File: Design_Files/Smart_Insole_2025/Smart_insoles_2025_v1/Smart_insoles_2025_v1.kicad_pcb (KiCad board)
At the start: 4 copper layers, 69.7 x 30.1 mm, 88 parts, among them IC1 USBLC6-2SC6, J1 Conn_01x20, J2 USB_C_Receptacle_USB2.0_16P, J4 S2B-PH-SM4-TB_LF__SN_, Q2 FDN306P, SW1 RESET, SW2 BOOT, SW3 SW_Nidec_CAS-120A1, U1 ME6211C33M5, U2 CD74HC4067M96, U3 LSM6DSO32TR, U5 ESP32-C3-MINI-1-N4, U7 BQ24040DSQR, U8 MCP6004-I_ST, U9 MCP6004-I_ST

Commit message: PCB:new routing-p1
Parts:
- C14, C15, C24, RN1, U3: moved to B.Cu
- moved J4 45.5 mm to (115.5, 83.7)
- moved SW3 24.8 mm to (154.8, 96.9), turned to 180 degrees
- moved C22 19.8 mm to (141.2, 83.2)
- moved D2 19.8 mm to (150.2, 83.2)
- moved R28 19.8 mm to (147.7, 83.2)
- moved U1 19.8 mm to (144.6, 83.2)
- moved C23 19.8 mm to (144.7, 86.2)
- moved R13 19.4 mm to (123.3, 89.5)
- moved R27 19.4 mm to (123.3, 87.5)
- moved JP2 18.1 mm to (124.5, 92.5)
- moved C16 17.7 mm to (129.2, 89.6)
- moved C19 17.7 mm to (133.4, 87.0)
- moved R20 17.7 mm to (138.2, 87.0)
- moved R21 17.7 mm to (135.8, 87.0)
- moved D1 17.7 mm to (135.8, 83.3)
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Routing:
- net +3V3: track 55.8 -> 117.3 mm, vias 0 -> 3
- net /FSR_AnalogFE/FSR_OUT_7: track 76.8 -> 15.8 mm, vias 2 -> 0
- net /FSR_AnalogFE/FSR_OUT_6: track 65.2 -> 14.9 mm
- net GND: track 159.3 -> 121.9 mm, vias 84 -> 74
- net I7: track 11.1 -> 45.7 mm, vias 1 -> 4
- net VBUS: track 54.8 -> 22.2 mm
- net /Battery Circuit Options/VBat: track 19.7 -> 49.1 mm
- net /FSR_AnalogFE/FSR_OUT_5: track 43.9 -> 19.5 mm
- net S1: track 2.04 -> 24.5 mm, vias 1 -> 0
- net S0: track 2.00 -> 22.6 mm, vias 1 -> 0
- net /FSR_AnalogFE/FSR_OUT_4: track 30.5 -> 10.8 mm
- net /Battery Circuit Options/~{PG}: track 0.00 -> 18.9 mm
- net S2: track 22.1 -> 4.63 mm
- net S3: track 22.1 -> 4.74 mm
- net /FSR_AnalogFE/FSR_OUT_0: track 29.0 -> 15.5 mm
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
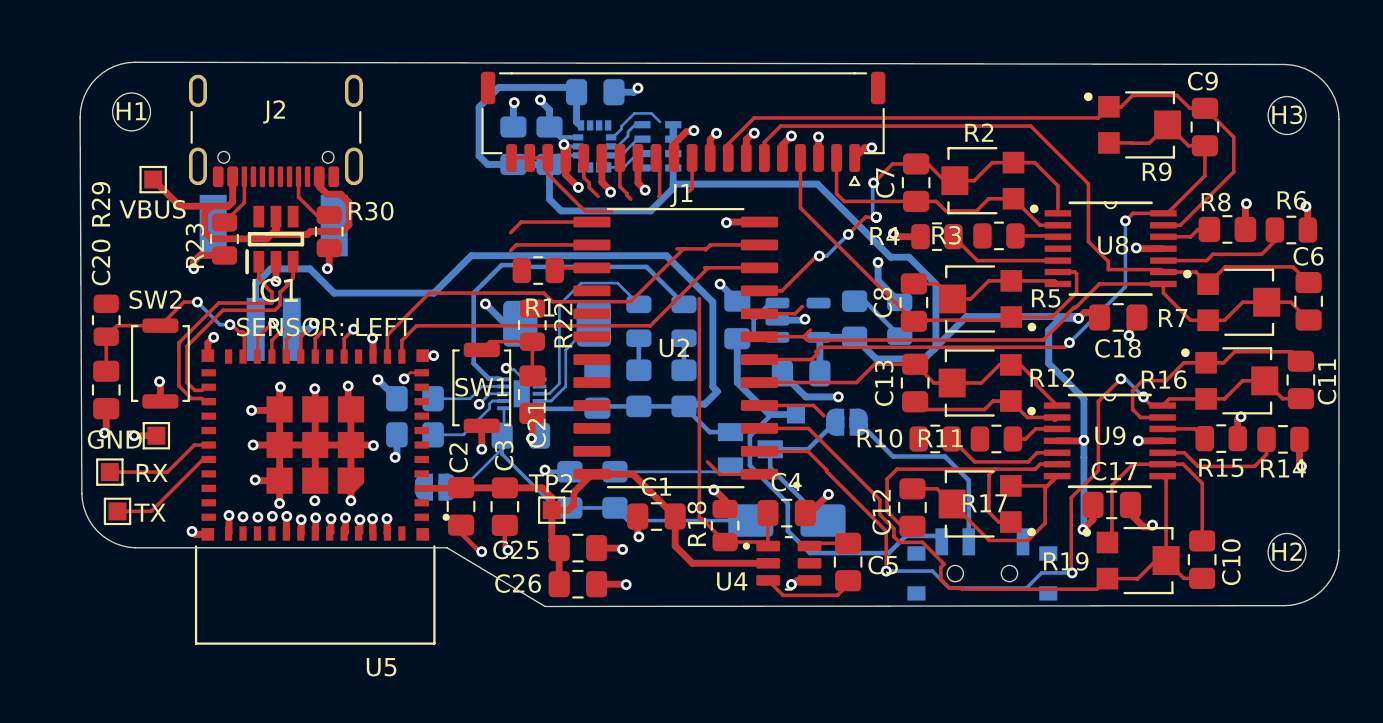
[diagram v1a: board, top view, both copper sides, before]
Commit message: PCB: finished routing single ended signal. Pending usb differential pair
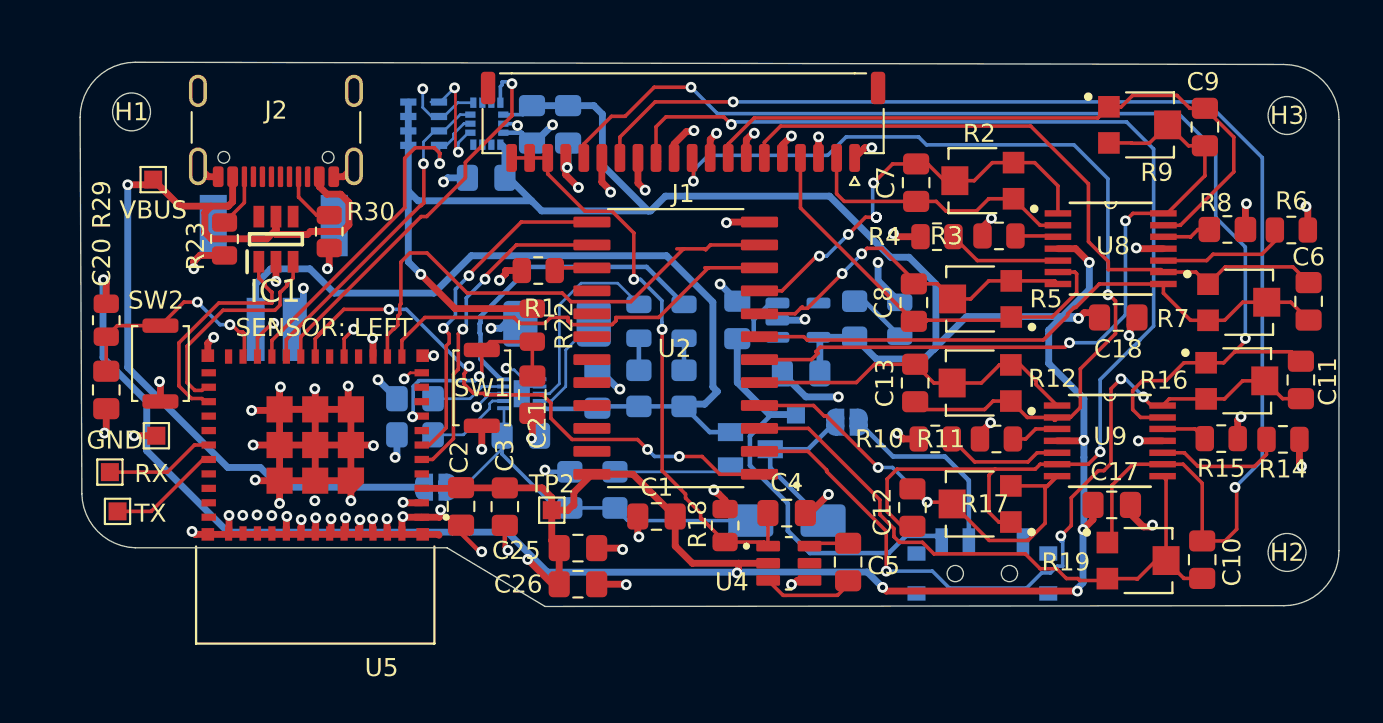
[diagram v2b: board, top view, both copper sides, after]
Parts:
- moved RN1 13.0 mm to (123.8, 72.3), turned to 180 degrees
- moved C24 7.68 mm to (127.3, 75.3), turned to 180 degrees
- moved U3 6.10 mm to (127.3, 72.3), turned to -90 degrees
- moved C14 3.25 mm to (131.8, 72.4), turned to -90 degrees
- moved C15 1.53 mm to (129.8, 72.4), turned to -90 degrees
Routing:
- net +3V3: track 117.3 -> 212.8 mm, vias 3 -> 10
- net /FSR_AnalogFE/FSR_OUT_6: track 14.9 -> 74.6 mm, vias 0 -> 2
- net /FSR_AnalogFE/FSR_OUT_5: track 19.5 -> 68.7 mm, vias 0 -> 2
- net /FSR_AnalogFE/FSR_OUT_7: track 15.8 -> 63.9 mm, vias 0 -> 2
- net /FSR_AnalogFE/FSR_OUT_4: track 10.8 -> 50.9 mm, vias 0 -> 2
- net GND: track 121.9 -> 158.4 mm, vias 74 -> 85
- net VBUS: track 22.2 -> 53.0 mm, vias 0 -> 1
- net SIG: track 4.68 -> 31.9 mm, vias 0 -> 4
- net INT: track 1.55 -> 22.0 mm, vias 0 -> 1
- net SCL: track 4.14 -> 20.5 mm, vias 0 -> 1
- net SDA: track 3.44 -> 18.3 mm, vias 0 -> 1
- net S3: track 4.74 -> 19.1 mm, vias 0 -> 2
- net S2: track 4.63 -> 18.8 mm, vias 0 -> 2
- net I1: track 11.3 -> 19.9 mm, vias 0 -> 2
- net I5: track 18.4 -> 26.1 mm, vias 0 -> 2
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
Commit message: SCH:Added pullup resistors on strapping pins.Added 0.1uF on analog input. Added testpoint on missing pad. PCB:Placed new components.Routing refactoring p1
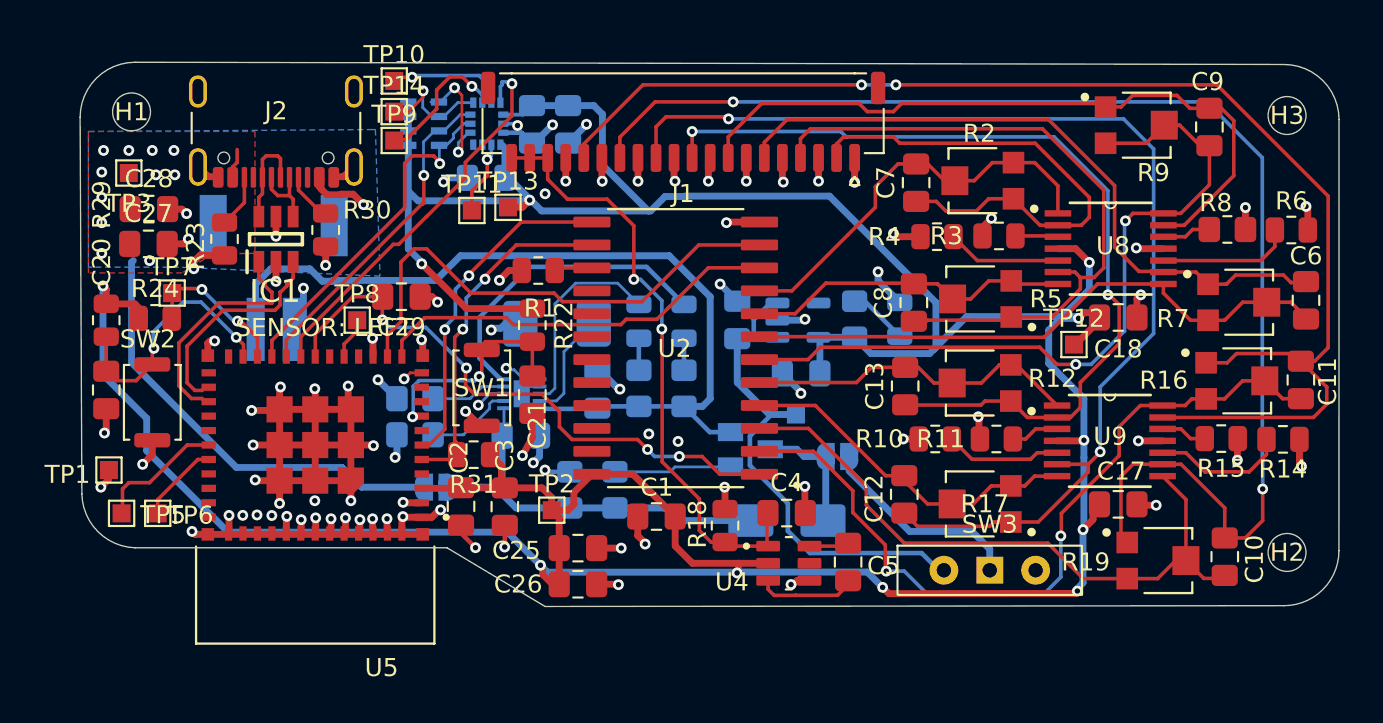
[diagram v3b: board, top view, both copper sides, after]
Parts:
- added C27: 0.1uF, Capacitor_SMD:C_0805_2012Metric_Pad1.18x1.45mm_HandSolder, F.Cu at (108.6, 79.0)
- added C28: 10uF, Capacitor_SMD:C_0805_2012Metric_Pad1.18x1.45mm_HandSolder, F.Cu at (108.6, 77.0)
- added C29: 0.1uF, Capacitor_SMD:C_0805_2012Metric_Pad1.18x1.45mm_HandSolder, F.Cu at (122.6, 81.9)
- added R24: 10k, Resistor_SMD:R_0805_2012Metric, F.Cu at (109.0, 83.1)
- added R31: 10k, Resistor_SMD:R_0805_2012Metric, F.Cu at (126.6, 90.7)
- added TP10: TestPoint_Alt, TestPoint:TestPoint_Pad_1.0x1.0mm, F.Cu at (122.2, 70.0)
- added TP11: TestPoint_Alt, TestPoint:TestPoint_Pad_1.0x1.0mm, F.Cu at (126.5, 77.1)
- added TP12: TestPoint_Alt, TestPoint:TestPoint_Pad_1.0x1.0mm, F.Cu at (159.8, 84.5)
- added TP13: TestPoint_Alt, TestPoint:TestPoint_Pad_1.0x1.0mm, F.Cu at (128.5, 77.0)
- added TP14: TestPoint_Alt, TestPoint:TestPoint_Pad_1.0x1.0mm, F.Cu at (122.2, 71.7)
- added TP7: TestPoint_Alt, TestPoint:TestPoint_Pad_1.0x1.0mm, F.Cu at (109.9, 81.7)
- added TP8: TestPoint_Alt, TestPoint:TestPoint_Pad_1.0x1.0mm, F.Cu at (120.2, 83.2)
- added TP9: TestPoint_Alt, TestPoint:TestPoint_Pad_1.0x1.0mm, F.Cu at (122.2, 73.2)
- C21: value 0.1uF -> 1uF
- SW3: footprint Button_Switch_SMD:SW_SPDT_PCM12 -> Button_Switch_THT:SW_Slide-03_Wuerth-WS-SLTV_10x2.5x6.4_P2.54mm; moved to F.Cu
- moved TP1 3.24 mm to (106.4, 91.5)
- moved TP5 2.38 mm to (107.1, 93.9)
- moved TP6 2.23 mm to (109.1, 93.9)
- moved SW2 2.19 mm to (108.8, 87.8)
- moved JP1 1.97 mm to (146.8, 90.8)
- moved TP3 1.40 mm to (107.5, 75.0)
- moved C10 1.26 mm to (168.2, 96.3)
- moved R19 1.10 mm to (164.6, 96.5)
- moved C12 0.86 mm to (150.4, 92.8)
- moved C13 0.58 mm to (150.5, 86.8)
- moved SW3 0.43 mm to (155.2, 97.0), turned to 0 degrees
- moved C17 0.36 mm to (162.3, 93.4)
- moved C9 0.25 mm to (167.3, 72.5)
- moved R30 0.22 mm to (118.4, 78.2)
- moved R9 0.19 mm to (163.4, 72.4)
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- renumbered GND to TP1, VBUS to TP3, RX to TP5, TX to TP6
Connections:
- net /Battery Circuit Options/IN renamed /Battery Circuit Options/VBUS_IN
- net Net-(D5-K) renamed /Battery Circuit Options/VBUS_OUT_A
- net Net-(JP1-B) renamed /Battery Circuit Options/VBUS_OUT_B
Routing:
- net VBUS: track 53.0 -> 31.0 mm, vias 1 -> 13
- net /FSR_AnalogFE/FSR_OUT_1: track 23.4 -> 37.3 mm
- net /FSR_AnalogFE/FSR_OUT_0: track 15.5 -> 28.3 mm
- net /FSR_AnalogFE/FSR_OUT_7: track 63.9 -> 74.2 mm
- net SDX: track 0.00 -> 7.79 mm, vias 0 -> 1
- net SCX: track 0.00 -> 7.45 mm, vias 0 -> 1
- net I5: track 26.1 -> 19.2 mm, vias 2 -> 0
- net IO8: track 2.27 -> 8.46 mm, vias 1 -> 2
- net +3V3: track 212.8 -> 218.6 mm, vias 10 -> 11
- net /USB_TVS_P: track 0.00 -> 5.40 mm
- net /FSR_AnalogFE/FSR_OUT_5: track 68.7 -> 63.9 mm
- net /USB_TVS_N: track 0.00 -> 4.13 mm
- net INT2: track 0.00 -> 4.09 mm, vias 0 -> 1
- net GND: track 158.4 -> 155.7 mm, vias 85 -> 92
- net /Battery Circuit Options/VBUS_OUT_A: track 9.38 -> 6.85 mm
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- added copper zone on B.Cu, net VBUS
- added copper zone on F.Cu, net VBUS

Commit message: PCB: Routing refactoring. Moved Multiplexer to the right. Organized Silkscreen p1. USB DIFF NOT READY
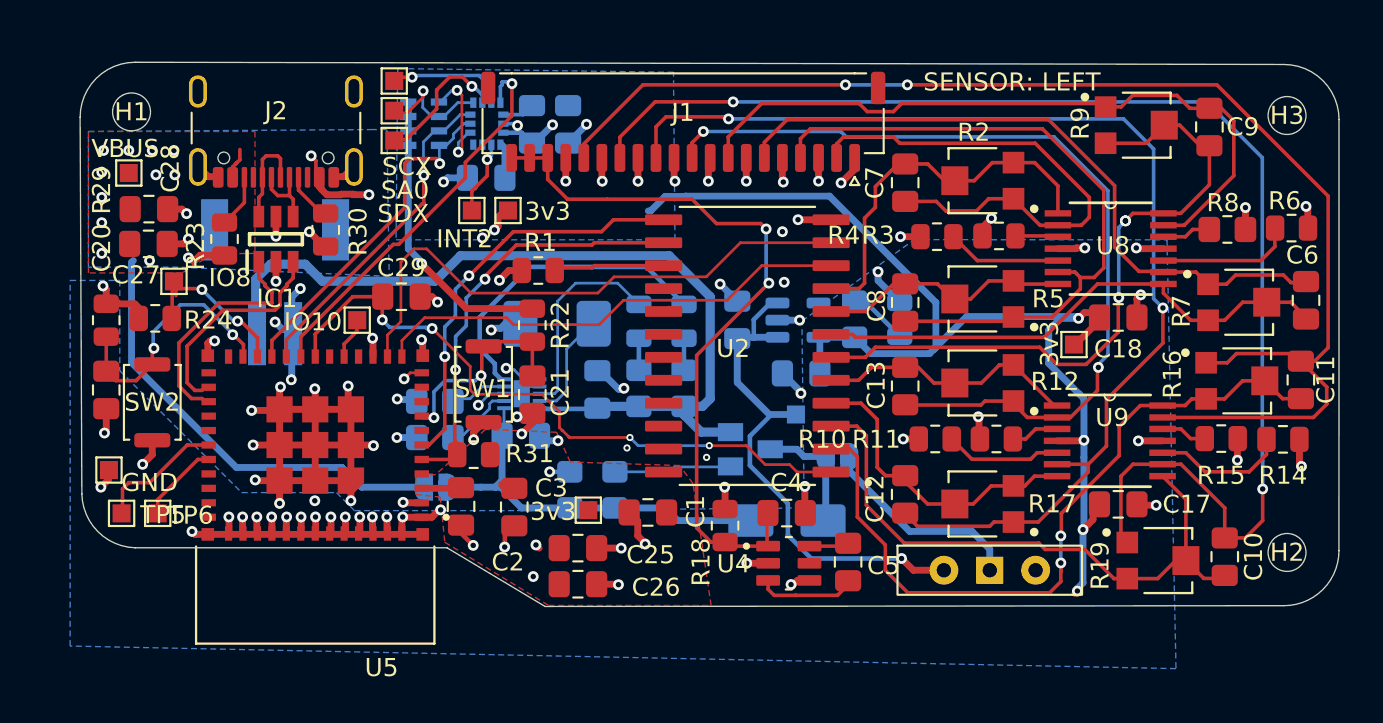
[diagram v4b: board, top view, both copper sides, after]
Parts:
- moved U2 3.97 mm to (141.8, 84.6)
- moved 3v3 2.02 mm to (132.9, 93.7)
- moved R13 1.11 mm to (124.5, 89.7)
- moved R27 1.11 mm to (124.5, 87.7)
- moved IO8 0.66 mm to (110.0, 81.0)
- moved C7 0.61 mm to (150.5, 75.6)
- moved C1 0.53 mm to (136.2, 93.8)
- moved C3 0.53 mm to (128.8, 93.5)
- moved C8 0.48 mm to (150.5, 82.2)
- moved J4 0.25 mm to (115.6, 84.0)
- moved SW1 0.22 mm to (127.2, 86.8)
- moved 3v3 0.17 mm to (128.5, 77.1)
- moved R12 0.15 mm to (154.7, 86.7)
- moved R17 0.15 mm to (154.7, 93.4)
- moved R5 0.12 mm to (154.7, 82.0)
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- renumbered TP13 to 3v3, TP2 to 3v3, TP12 to 3v3, TP1 to GND, TP11 to INT2, TP8 to IO10, TP7 to IO8, TP14 to SA0, TP10 to SCX, TP9 to SDX, TP3 to VBUS
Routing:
- net +3V3: track 218.6 -> 95.7 mm
- net /FSR_AnalogFE/FSR_IN: track 33.8 -> 41.0 mm
- net GND: track 155.7 -> 162.8 mm, vias 92 -> 97
- net I1: track 18.3 -> 14.0 mm
- net I3: track 42.1 -> 37.9 mm, vias 2 -> 3
- net SIG: track 32.7 -> 36.8 mm
- net S3: track 18.9 -> 22.9 mm
- net Net-(U2-~{E}): track 2.12 -> 6.14 mm
- net I4: track 18.5 -> 14.5 mm
- net S0: track 22.7 -> 26.7 mm
- net I2: track 33.5 -> 29.6 mm
- net S2: track 19.5 -> 23.4 mm
- net S1: track 28.2 -> 31.8 mm
- net I5: track 19.2 -> 16.8 mm
- net I6: track 35.9 -> 33.7 mm
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- added copper zone on B.Cu, net +3V3
- added copper zone on F.Cu, net +3V3

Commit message: PCB: Added power puddles on Vbat,3v3, VBUS
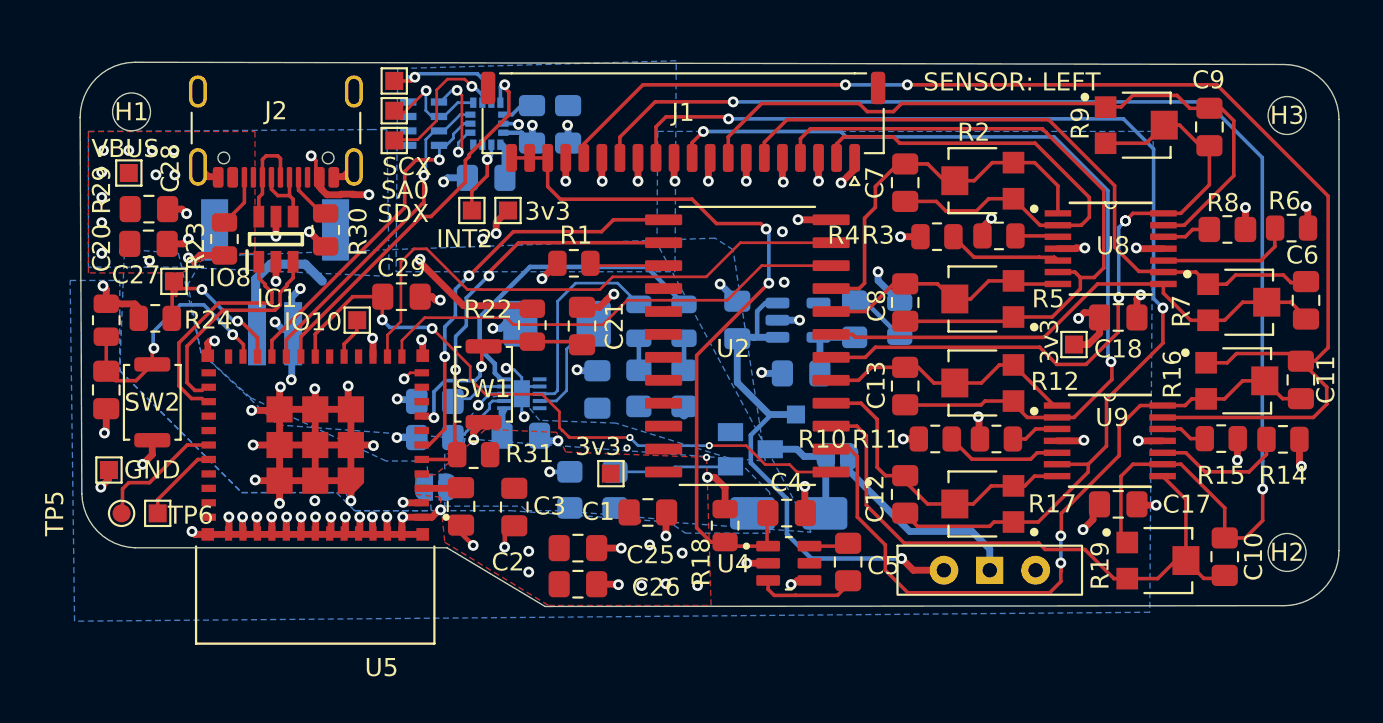
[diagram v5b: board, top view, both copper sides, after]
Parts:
- TP5: footprint TestPoint:TestPoint_Pad_1.0x1.0mm -> TestPoint:TestPoint_Pad_D1.0mm
- moved C21 4.69 mm to (132.6, 83.5), turned to -90 degrees
- moved 3v3 2.38 mm to (134.2, 91.7)
- moved R1 2.01 mm to (132.2, 80.0)
- moved D5 0.41 mm to (144.1, 93.9)
- turned C1 to 0 degrees
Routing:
- net +3V3: track 95.7 -> 34.7 mm, vias 11 -> 15
- net /Battery Circuit Options/VBat: track 49.3 -> 8.13 mm
- net VBUS: track 32.6 -> 6.06 mm
- net /Battery Circuit Options/VBUS_IN: track 23.6 -> 2.03 mm
- net Net-(U2-~{E}): track 6.14 -> 3.96 mm
- net GND: track 162.8 -> 161.3 mm
- net Net-(U5-EN): track 11.7 -> 12.5 mm
- net SCL: track 19.4 -> 18.9 mm
- added copper zone on B.Cu, net /Battery Circuit Options/VBUS_IN
- added copper zone on B.Cu, net /Battery Circuit Options/VBat

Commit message: PCB:USB Differential pair Impedance calculation and Routing. Also Organized Silkscreen. Added text polarity to battery, boot and rst buttons, and RX TX
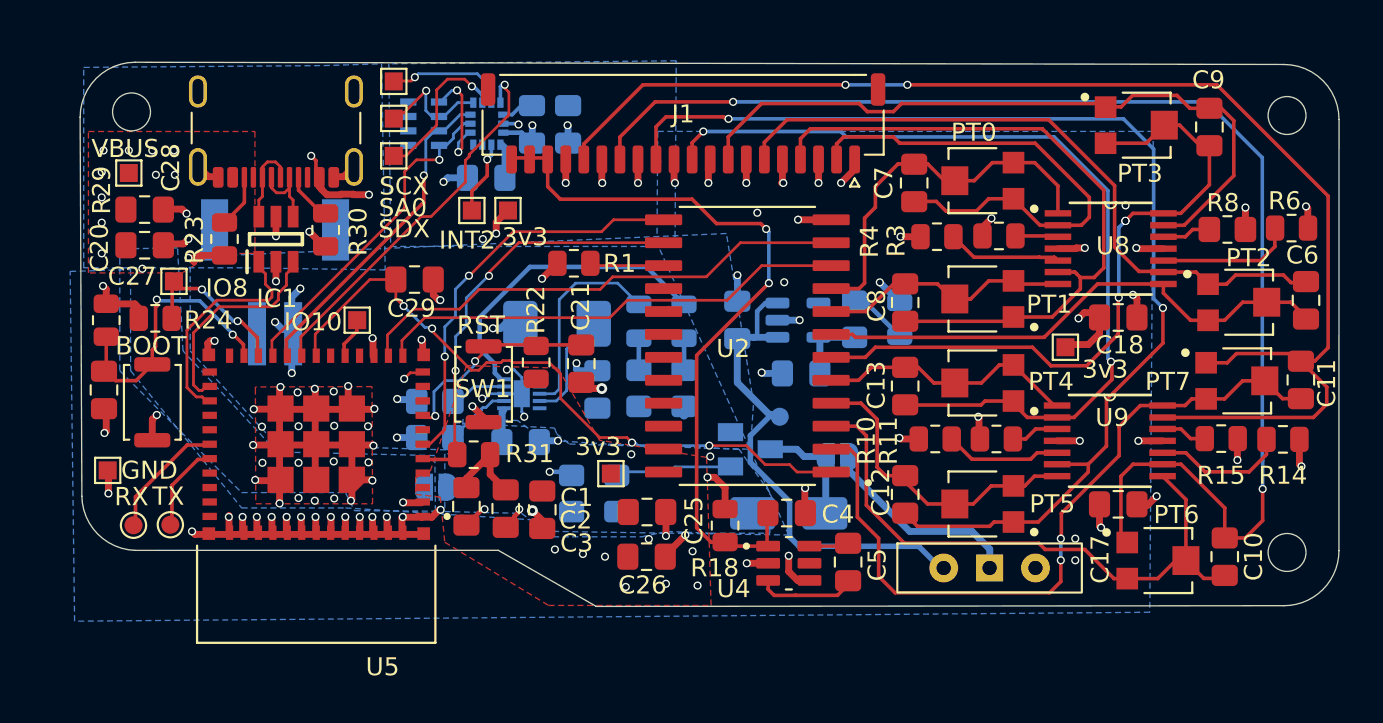
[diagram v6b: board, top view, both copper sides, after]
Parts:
- TP6: footprint TestPoint:TestPoint_Pad_1.0x1.0mm -> TestPoint:TestPoint_Pad_D1.0mm
- VSEL: renamed from TP4; footprint TestPoint:TestPoint_Pad_1.0x1.0mm -> TestPoint:TestPoint_Pad_D1.0mm
- moved C1 7.88 mm to (128.4, 93.6), turned to -90 degrees
- moved C25 4.32 mm to (136.2, 93.8)
- moved C26 4.09 mm to (136.2, 96.3)
- moved C21 2.08 mm to (132.6, 85.6), turned to 90 degrees
- moved R22 2.07 mm to (130.1, 85.5), turned to 90 degrees
- moved C3 1.56 mm to (130.4, 93.7)
- moved C29 1.20 mm to (123.3, 81.0)
- moved TP6 0.94 mm to (109.8, 94.5)
- moved TP5 0.93 mm to (107.8, 94.6)
- moved VSEL 0.91 mm to (143.6, 88.5)
- moved SDX 0.85 mm to (122.2, 74.1)
- moved C7 0.50 mm to (151.0, 75.6)
- moved 3v3 0.50 mm to (159.4, 84.7)
- moved SA0 0.43 mm to (122.2, 72.0)
- moved C16 0.35 mm to (129.2, 90.0)
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- renumbered R2 to PT0, R5 to PT1, R7 to PT2, R9 to PT3, R12 to PT4, R17 to PT5, R19 to PT6, R16 to PT7
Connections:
- net Net-(U5-EN) renamed /EN
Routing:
- net /Battery Circuit Options/VBat: track 8.13 -> 0.76 mm
- net +3V3: track 34.7 -> 28.6 mm
- net S1: track 31.7 -> 27.9 mm
- net GND: track 161.3 -> 158.6 mm, vias 97 -> 114
- net Vsel: track 31.1 -> 29.3 mm, vias 1 -> 0
- net SIG: track 36.4 -> 37.9 mm
- net Net-(U5-IO9): track 14.1 -> 15.5 mm
- net SCX: track 7.68 -> 6.73 mm
- net /USB_TVS_P: track 5.40 -> 4.64 mm
- net /USB_P: track 13.1 -> 12.5 mm
- net /EN: track 12.5 -> 12.0 mm
- net SDX: track 8.07 -> 8.60 mm
- net /USB_TVS_N: track 4.13 -> 4.64 mm
- added copper zone on F.Cu, net GND
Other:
- outline, holes or cut-outs redrawn
- board text added: "+"
- board text added: "-"
- board text added: "BOOT"
- board text added: "FPUNE-GEAR Insole_V1.0 / REV A 12/2025 Ing. René A."
- board text added: "RST"
- board text added: "RX"
- board text added: "TX"
- board text removed: "FPUNE-GEAR Insole_V0.01 05/2025"
